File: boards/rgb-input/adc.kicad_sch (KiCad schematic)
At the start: 9 parts, among them U13 MCP1502, U2 MCP3208, U4 MCP3221A0T

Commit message: some adc changes and then rerouting
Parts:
- removed U4: MCP3221A0T, Package_TO_SOT_SMD:SOT-23-5, symbol gnarboard:MCP3X21
- added C3: 10uF, Capacitor_SMD:C_0805_2012Metric_Pad1.18x1.45mm_HandSolder, symbol Device:C_Small
- added D39: BAT54S, Package_TO_SOT_SMD:SOT-23, symbol Diode:BAT54S
- added JP1: SolderJumper_2_Open, Jumper:SolderJumper-2_P1.3mm_Open_RoundedPad1.0x1.5mm, symbol Jumper:SolderJumper_2_Open
- added U15: MCP3425A0T-ECH, Package_TO_SOT_SMD:SOT-23-6, symbol Analog_ADC:MCP3425A0T-ECH
- R33: value 130K 0.1% -> 300K 0.1%
- R34: value 15K 0.1% -> 22K 0.1%
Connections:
- net +3.3V: now also JP1.2 (B); no longer C3.1, U13.4 (~{SHDN}), U13.6 (VDD)
- net GNDA: now also C3.2, D39.1 (A), U15.2 (Vss), U15.6 (Vin-)
- net REF_3V3: now also C3.1, D39.2 (K), JP1.1 (A), U15.5 (Vdd)
- net SCL: now also U15.4 (SDA)
- net SDA: now also U15.3 (SCL)
- net at R33.1, R34.2: now also D39.3 (COM), U15.1 (Vin+)
- new net ESP32_5V: C3.1, U13.4 (~{SHDN}), U13.6 (VDD)
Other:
- note added: "Bus Voltage Circuit"
- note added: "Reference Voltage Circuit"
- moved on the sheet: C3, R33, R34, U13, U2

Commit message: too much routing
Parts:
- removed C3: 10uF, Capacitor_SMD:C_0805_2012Metric_Pad1.18x1.45mm_HandSolder, symbol Device:C_Small
- removed C3: 100nF, Capacitor_SMD:C_0805_2012Metric_Pad1.18x1.45mm_HandSolder, symbol Device:C_Small
- removed D39: BAT54S, Package_TO_SOT_SMD:SOT-23, symbol Diode:BAT54S
- removed R33: 300K 0.1%, Resistor_SMD:R_0805_2012Metric_Pad1.20x1.40mm_HandSolder, symbol Device:R_Small_US
- removed R34: 22K 0.1%, Resistor_SMD:R_0805_2012Metric_Pad1.20x1.40mm_HandSolder, symbol Device:R_Small_US
- removed U15: MCP3425A0T-ECH, Package_TO_SOT_SMD:SOT-23-6, symbol Analog_ADC:MCP3425A0T-ECH
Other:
- note removed: "Bus Voltage Circuit"
- moved on the sheet: U2

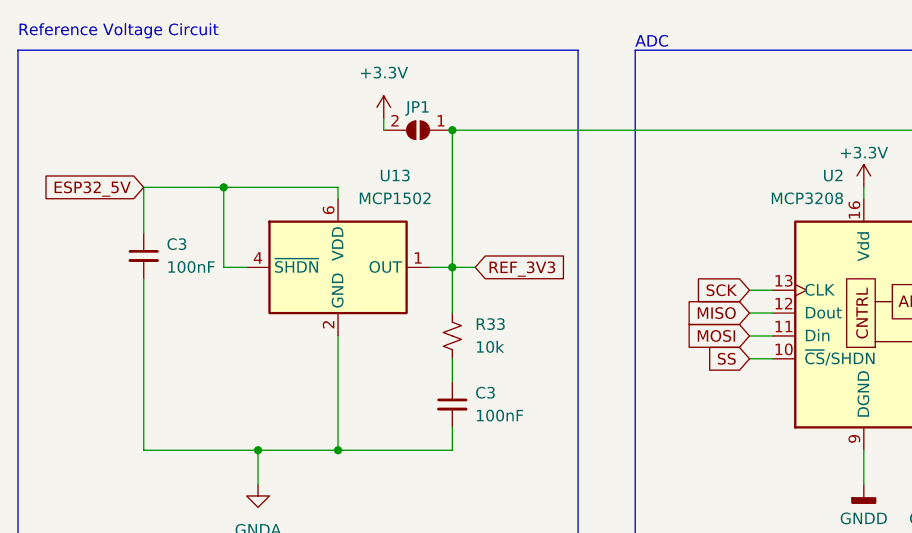
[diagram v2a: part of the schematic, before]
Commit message: whoa, board is fully routed!!!!
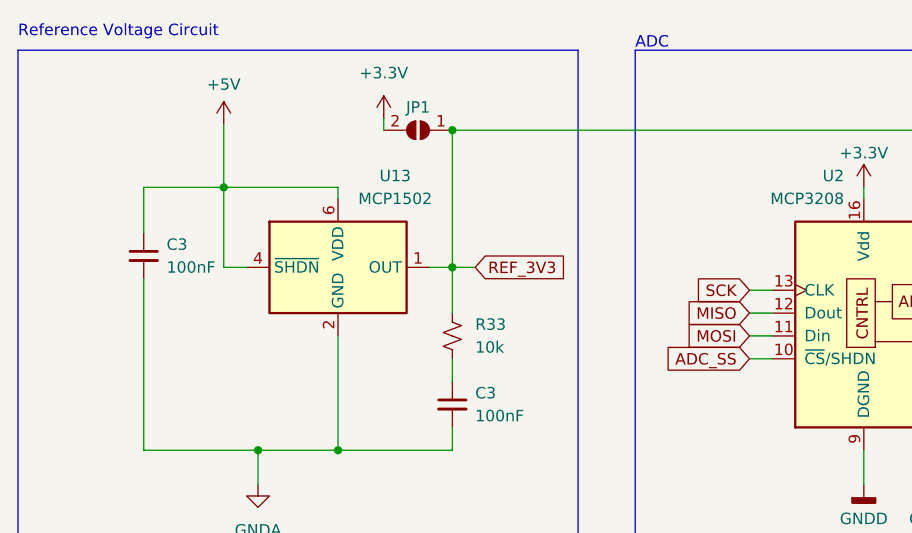
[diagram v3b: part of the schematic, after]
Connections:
- net ESP32_5V renamed +5V
- net SS renamed ADC_SS
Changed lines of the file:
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@@
+    (stroke (width 0) (type default))
+  )
+  (wire (pts (xy 58.42 66.675) (xy 58.42 73.66))
     (stroke (width 0) (type default))
   )
@@
     )
   )
-  (global_label "ESP32_5V" (shape input) (at 49.53 73.66 180) (fields_autoplaced)
-    (effects (font (size 1.27 1.27)) (justify right))
-    (property "Intersheetrefs" "${INTERSHEET_REFS}" (at 37.2316 73.66 0)
-      (effects (font (size 1.27 1.27)) (justify right) hide)
-    )
-  )
   (global_label "MOSI" (shape input) (at 116.84 90.17 180) (fields_autoplaced)
     (effects (font (size 1.27 1.27)) (justify right))
@@
     )
   )
-  (global_label "SS" (shape input) (at 116.84 92.71 180) (fields_autoplaced)
+  (global_label "ADC_SS" (shape input) (at 116.84 92.71 180) (fields_autoplaced)
     (effects (font (size 1.27 1.27)) (justify right))
-    (property "Intersheetrefs" "${INTERSHEET_REFS}" (at 111.4358 92.71 0)
+    (property "Intersheetrefs" "${INTERSHEET_REFS}" (at 106.8396 92.71 0)
       (effects (font (size 1.27 1.27)) (justify right) hide)
     )
@@
         )
       )
+    )
+  )
+  (symbol (lib_id "power:+5V") (at 58.42 66.675 0) (unit 1)
+    (in_bom yes) (on_board yes) (dnp no) (fields_autoplaced)
+    (property "Reference" "#PWR066" (at 58.42 70.485 0)
+      (effects (font (size 1.27 1.27)) hide)
+    )
+    (property "Value" "+5V" (at 58.42 62.23 0)
+      (effects (font (size 1.27 1.27)))
+    )
+    (property "Footprint" "" (at 58.42 66.675 0)
+      (effects (font (size 1.27 1.27)) hide)
+    )
+    (property "Datasheet" "" (at 58.42 66.675 0)
+      (effects (font (size 1.27 1.27)) hide)
+    )
+    (pin "1")
+    (instances
+      (project "rgb-input"
+        (path "/c83c6236-96e9-46ad-9d7a-9e2efa4a7966/b87f80e1-ecbd-4ee0-be26-4b252158928b"
+          (reference "#PWR066") (unit 1)
+        )
+      )

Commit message: more BOM updates.
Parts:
- C3: Vendor C0805C102J1HACTU -> (none)
- JP1: now not fitted; now left out of the parts list
- R33: Vendor 652-CR0805JW-104ELF -> (none)
- U13: Mouser (none) -> 579-MCP1502T-33E/CHY
- U2: Mouser (none) -> 579-MCP3208T-BI/SL; Vendor MCP3208T-BI/SL -> (none)
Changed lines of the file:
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@@
       (effects (font (size 1.27 1.27)) hide)
     )
-    (property "Vendor" "MCP3208T-BI/SL" (at 134.62 87.63 0)
+    (property "Mouser" "579-MCP3208T-BI/SL" (at 134.62 87.63 0)
       (effects (font (size 1.27 1.27)) hide)
     )
@@
       (effects (font (size 1.27 1.27)) hide)
     )
-    (property "Vendor" "652-CR0805JW-104ELF" (at 83.82 90.17 0)
-      (effects (font (size 1.27 1.27)) hide)
-    )
     (pin "1")
     (pin "2")
@@
     )
     (property "Datasheet" "http://ww1.microchip.com/downloads/en/DeviceDoc/20005474E.pdf" (at 71.12 82.55 0)
+      (effects (font (size 1.27 1.27)) hide)
+    )
+    (property "Mouser" "579-MCP1502T-33E/CHY" (at 71.12 82.55 0)
       (effects (font (size 1.27 1.27)) hide)
     )
@@
       (effects (font (size 1.27 1.27)) hide)
     )
-    (property "Vendor" "C0805C102J1HACTU" (at 83.82 97.79 0)
-      (effects (font (size 1.27 1.27)) hide)
-    )
     (pin "1")
     (pin "2")
@@
   )
   (symbol (lib_id "Jumper:SolderJumper_2_Open") (at 80.01 67.31 180) (unit 1)
-    (in_bom yes) (on_board yes) (dnp no)
+    (in_bom no) (on_board yes) (dnp yes)
     (property "Reference" "JP1" (at 80.01 64.77 0)
       (effects (font (size 1.27 1.27)))
@@
       (effects (font (size 1.27 1.27)) hide)
     )
-    (property "Vendor" "C0805C102J1HACTU" (at 49.53 81.28 0)
-      (effects (font (size 1.27 1.27)) hide)
-    )

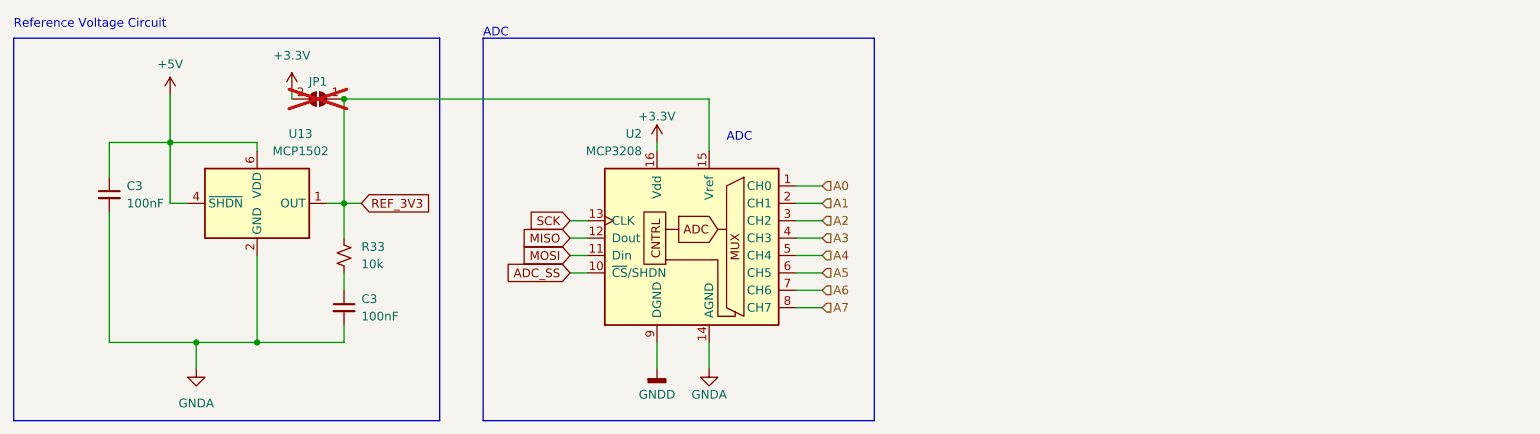
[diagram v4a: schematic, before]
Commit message: first pass on redesign of the rgb input board
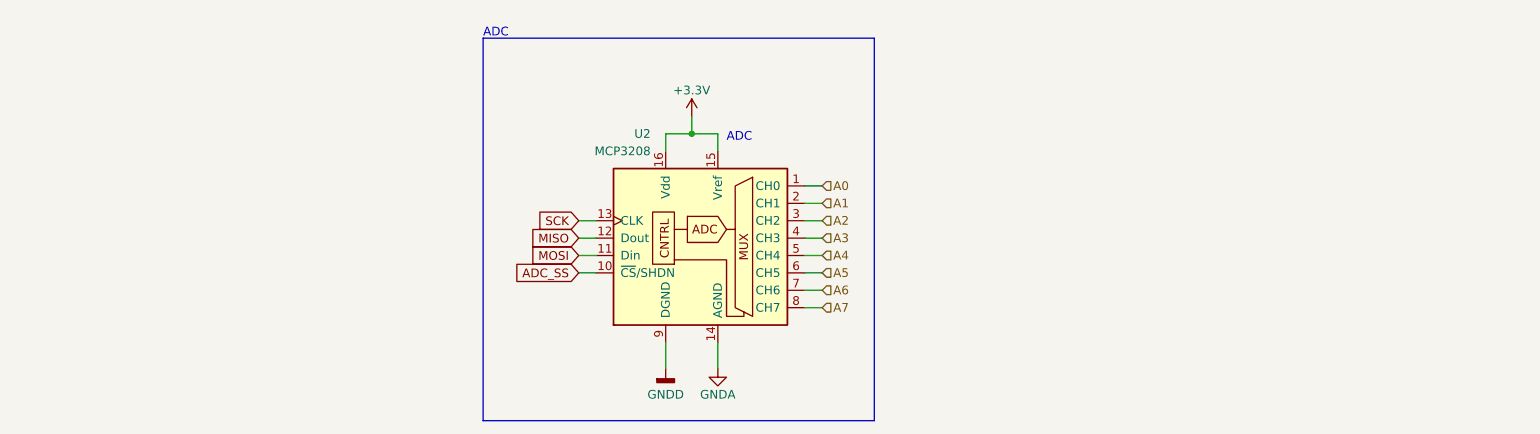
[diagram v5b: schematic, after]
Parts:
- removed C3 (x2): 100nF, Capacitor_SMD:C_0805_2012Metric_Pad1.18x1.45mm_HandSolder, symbol Device:C_Small
- removed JP1: SolderJumper_2_Open, Jumper:SolderJumper-2_P1.3mm_Open_RoundedPad1.0x1.5mm, symbol Jumper:SolderJumper_2_Open
- removed R33: 10k, Resistor_SMD:R_0805_2012Metric_Pad1.20x1.40mm_HandSolder, symbol Device:R_Small_US
- removed U13: MCP1502, Package_TO_SOT_SMD:SOT-23-6, symbol Reference_Voltage:MCP1501-30xCH
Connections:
- net REF_3V3 is gone; now on net +3.3V: U2.15 (Vref)
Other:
- note removed: "Reference Voltage Circuit"
- moved on the sheet: U2

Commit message: new rgb input board is starting to look very nice.
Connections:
- net MISO renamed ADC_MISO
- net MOSI renamed ADC_MOSI
- net SCK renamed ADC_SCK
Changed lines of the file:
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@@
     (effects (font (size 1.27 1.27)) (justify left bottom))
   )
-  (global_label "SCK" (shape input) (at 118.11 85.09 180) (fields_autoplaced)
+  (global_label "ADC_SCK" (shape input) (at 118.11 85.09 180) (fields_autoplaced)
     (effects (font (size 1.27 1.27)) (justify right))
-    (property "Intersheetrefs" "${INTERSHEET_REFS}" (at 111.3753 85.09 0)
+    (property "Intersheetrefs" "${INTERSHEET_REFS}" (at 106.7791 85.09 0)
       (effects (font (size 1.27 1.27)) (justify right) hide)
     )
   )
-  (global_label "MISO" (shape input) (at 118.11 87.63 180) (fields_autoplaced)
+  (global_label "ADC_MISO" (shape input) (at 118.11 87.63 180) (fields_autoplaced)
     (effects (font (size 1.27 1.27)) (justify right))
-    (property "Intersheetrefs" "${INTERSHEET_REFS}" (at 110.5286 87.63 0)
+    (property "Intersheetrefs" "${INTERSHEET_REFS}" (at 105.9324 87.63 0)
       (effects (font (size 1.27 1.27)) (justify right) hide)
     )
   )
-  (global_label "MOSI" (shape input) (at 118.11 90.17 180) (fields_autoplaced)
+  (global_label "ADC_MOSI" (shape input) (at 118.11 90.17 180) (fields_autoplaced)
     (effects (font (size 1.27 1.27)) (justify right))
-    (property "Intersheetrefs" "${INTERSHEET_REFS}" (at 110.5286 90.17 0)
+    (property "Intersheetrefs" "${INTERSHEET_REFS}" (at 105.9324 90.17 0)
       (effects (font (size 1.27 1.27)) (justify right) hide)
     )

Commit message: reannotated and did some more cleanup.  almost ready
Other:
- company: (none) -> github.com/hoeken/yarrboard
- title: (none) -> RGB Input Board
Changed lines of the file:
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@@
 (kicad_sch (version 20230121) (generator eeschema)
   (paper "A4")
+  (title_block
+    (title "RGB Input Board")
+    (rev "B")
+    (company "github.com/hoeken/yarrboard")
+    (comment 1 "Open Source Hardware")
+  )
   (junction (at 134.62 72.39) (diameter 0) (color 0 0 0 0)
   )
@@
         )
         (path "/c83c6236-96e9-46ad-9d7a-9e2efa4a7966/b87f80e1-ecbd-4ee0-be26-4b252158928b"
-          (reference "#PWR07") (unit 1)
+          (reference "#PWR030") (unit 1)
         )
       )
@@
         )
         (path "/c83c6236-96e9-46ad-9d7a-9e2efa4a7966/b87f80e1-ecbd-4ee0-be26-4b252158928b"
-          (reference "#PWR057") (unit 1)
+          (reference "#PWR028") (unit 1)
         )
       )
@@
         )
         (path "/c83c6236-96e9-46ad-9d7a-9e2efa4a7966/b87f80e1-ecbd-4ee0-be26-4b252158928b"
-          (reference "#PWR06") (unit 1)
-        )
-      )
+          (reference "#PWR029") (unit 1)
+        )
+      )
